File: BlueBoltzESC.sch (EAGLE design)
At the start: 86 parts, among them IC1 7805TV, Q1 BD679, Q2 BD679, Q3 BD679, Q4 IRLZ44Z, Q5 IRLZ44Z, Q6 IRLZ44Z, Q7 IRLZ44Z, Q8 IRLZ44Z, Q9 IRLZ44Z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

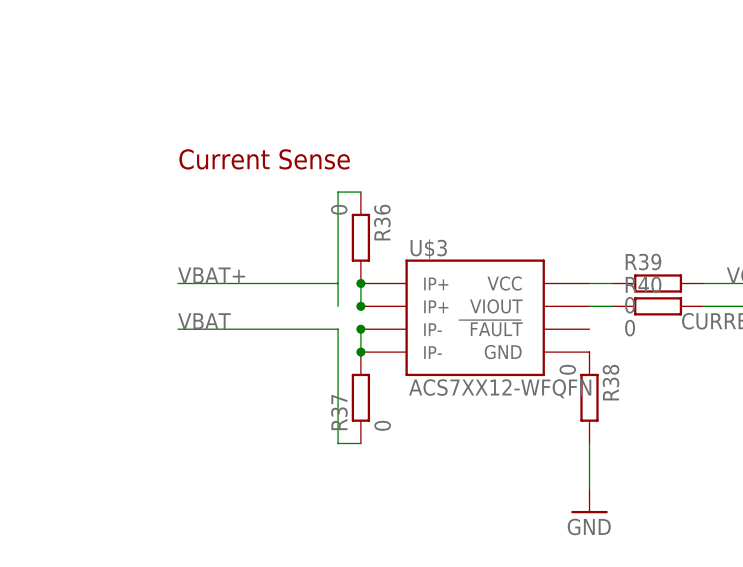
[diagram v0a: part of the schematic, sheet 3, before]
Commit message: Version 1.1 For BlueBoltzESC Board
In this Version, The board is updated with a single board footprint, which minimizes hassles...
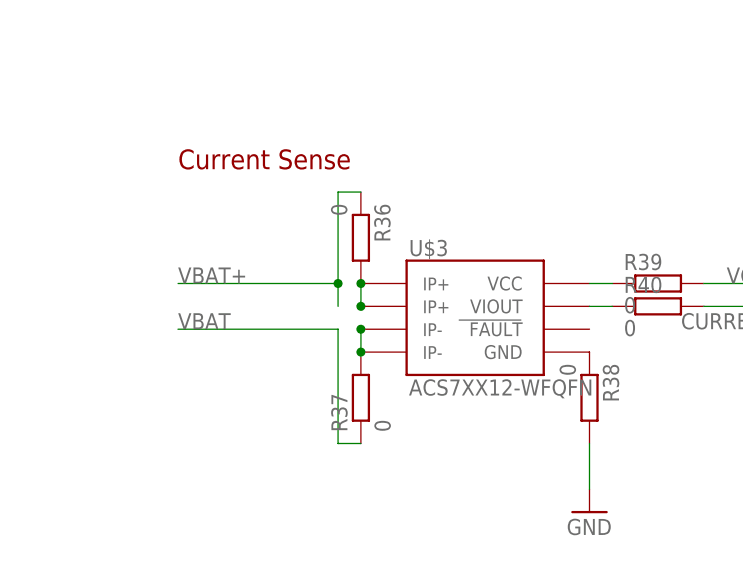
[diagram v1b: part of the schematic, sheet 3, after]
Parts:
- U1: SPICEPREFIX (none) -> X
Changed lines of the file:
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@@
 <?xml version="1.0" encoding="utf-8"?>
 <!DOCTYPE eagle SYSTEM "eagle.dtd">
-<eagle version="7.6.0">
+<eagle version="8.7.1">
 <drawing>
 <settings>
-<setting alwaysvectorfont="yes"/>
+<setting alwaysvectorfont="no"/>
+<setting keepoldvectorfont="yes"/>
 <setting verticaltext="up"/>
 </settings>
-<grid distance="0.05" unitdist="inch" unit="inch" style="lines" multiple="1" display="no" altdistance="0.05" altunitdist="inch" altunit="inch"/>
+<grid distance="0.1" unitdist="inch" unit="inch" style="lines" multiple="1" display="no" altdistance="0.01" altunitdist="inch" altunit="inch"/>
 <layers>
 <layer number="1" name="Top" color="4" fill="1" visible="no" active="no"/>
@@
 <part name="U$4" library="BR-Eagle-Library" deviceset="HEADER-6" device="2MM"/>
 <part name="U$8" library="BR-Eagle-Library" deviceset="HEADER-12" device="2MM"/>
-<part name="U1" library="SparkFun-DigitalIC" deviceset="ATMEGA168" device="" value="ATMEGA168"/>
+<part name="U1" library="SparkFun-DigitalIC" deviceset="ATMEGA168" device="" value="ATMEGA168">
+<attribute name="SPICEPREFIX" value="X"/>
+</part>
 <part name="R1" library="resistor" deviceset="R-US_" device="0207/10" value="47K"/>
 <part name="R2" library="resistor" deviceset="R-US_" device="0207/10" value="47K"/>
@@
 <pinref part="R36" gate="G$1" pin="1"/>
 <wire x1="38.1" y1="152.4" x2="40.64" y2="152.4" width="0.1524" layer="91"/>
-</segment>
-</net>
+<junction x="38.1" y="142.24"/>
+</segment>
+</net>

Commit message: Add files via upload
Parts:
- removed IC1: 7805TV, linear:7805TV
- removed U$3: ACS7XX12-WFQFN, BR-Eagle-Library:ACS7XX12-WFQFN
- added 5VREG, IC2: REG1117, burr-brown:REG1117
- added IC3: DC 2 AC 2, SamacSys_Parts:ACS712ELCTR-20A-T
- added J1: AVR_SPI_PROG_3X2NS, SparkFun-Connectors:AVR_SPI_PROG_3X2NS
- added SV1: (no value), con-lstb:MA03-1
- R33: device SparkFun-Resistors:33KOHM1/10W1%(0603) -> varistor:THERMISTOR-5
- U$16, U$4: value HEADER-62MM -> (none); device BR-Eagle-Library:HEADER-62MM -> con-lsta:FE06-1
- U$17, U$8: value HEADER-122MM -> (none); device BR-Eagle-Library:HEADER-122MM -> con-lsta:FE12-1
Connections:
- new net BEC+: IC2.VOUT, SV1.2
- net GND: now also IC2.GND, J1.6, R33.2, SV1.3; no longer R33.1
- net L_GND: now also 5VREG.GND; no longer IC1.GND
- net L_PWM_CL: now also J1.4
- net L_VBAT: now also 5VREG.VIN; no longer IC1.VI
- net MISO: now also J1.1
- net N$1: now also IC3.IP+, IC3.IP+_1; no longer U$3.IP+1, U$3.IP+2
- net N$13: now also IC3.GND; no longer U$3.GND
- net N$14: now also IC3.VCC; no longer U$3.VCC
- net N$17: now also IC3.VIOUT; no longer U$3.VIOUT
- net N$8: now also IC3.IP-, IC3.IP-_1; no longer U$3.IP-1, U$3.IP-2
- net PWM: now also SV1.1
- net RESET: now also J1.5
- net SCK: now also J1.3
- net TEMP_ADC: now also R33.1; no longer R33.2
- net VBAT+: now also IC2.VIN
- net VCC5V: now also 5VREG.VOUT, J1.2; no longer IC1.VO
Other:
- moved on the sheet: C10, R36, R38, R39, R40
